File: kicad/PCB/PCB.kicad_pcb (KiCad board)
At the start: 2 copper layers, 80 x 55 mm, 53 parts, among them J1 JST_2mm, J2 JST_2mm, J3 3.5mm, J5 3.5mm, J6 3.5mm, J7 3.5mm, J9 Selector_TC4420, Q1 IRL520N, SW1 SW_DIP_x03, U1 XIAO-RP2350-DIP, U2 AP2112K-3.3, U3 TB6612FNG, U4 TC4420

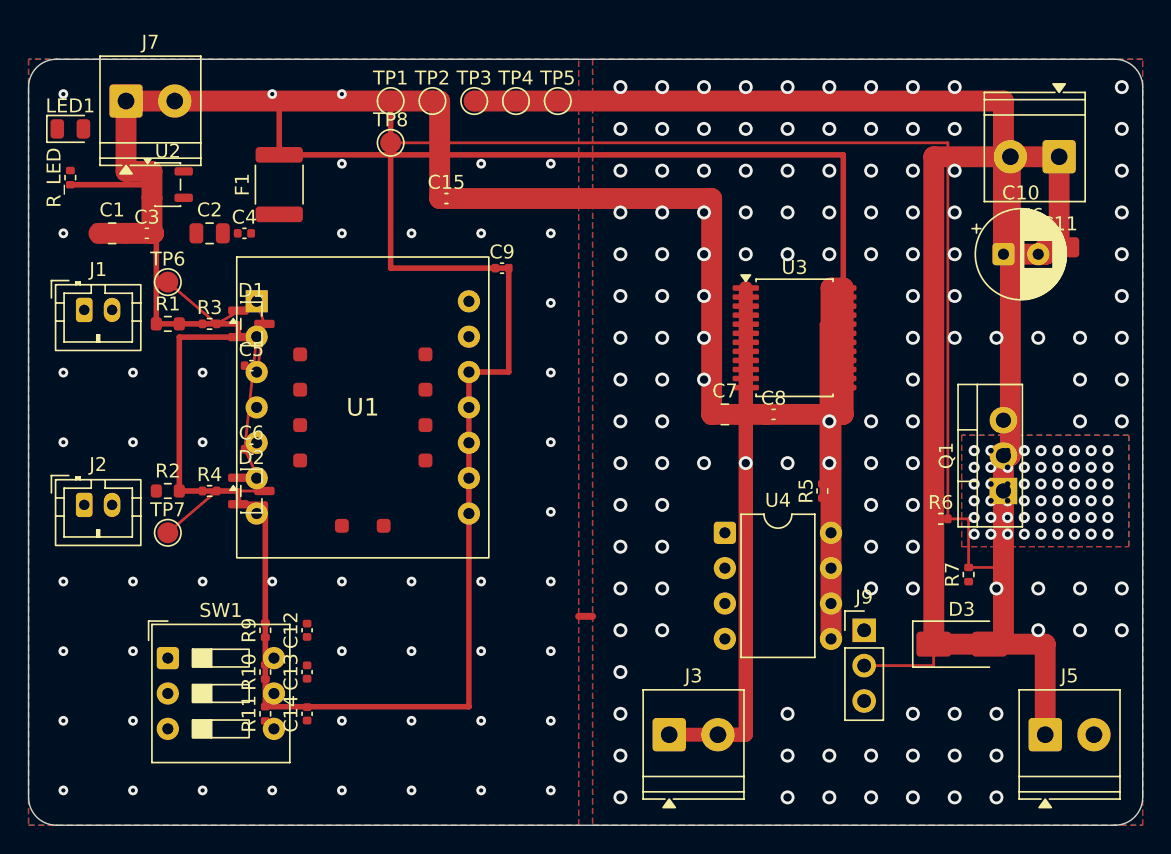
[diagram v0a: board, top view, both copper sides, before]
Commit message: Limpieza de archivos innecesarios de PCB y creacion de guia de enrutado
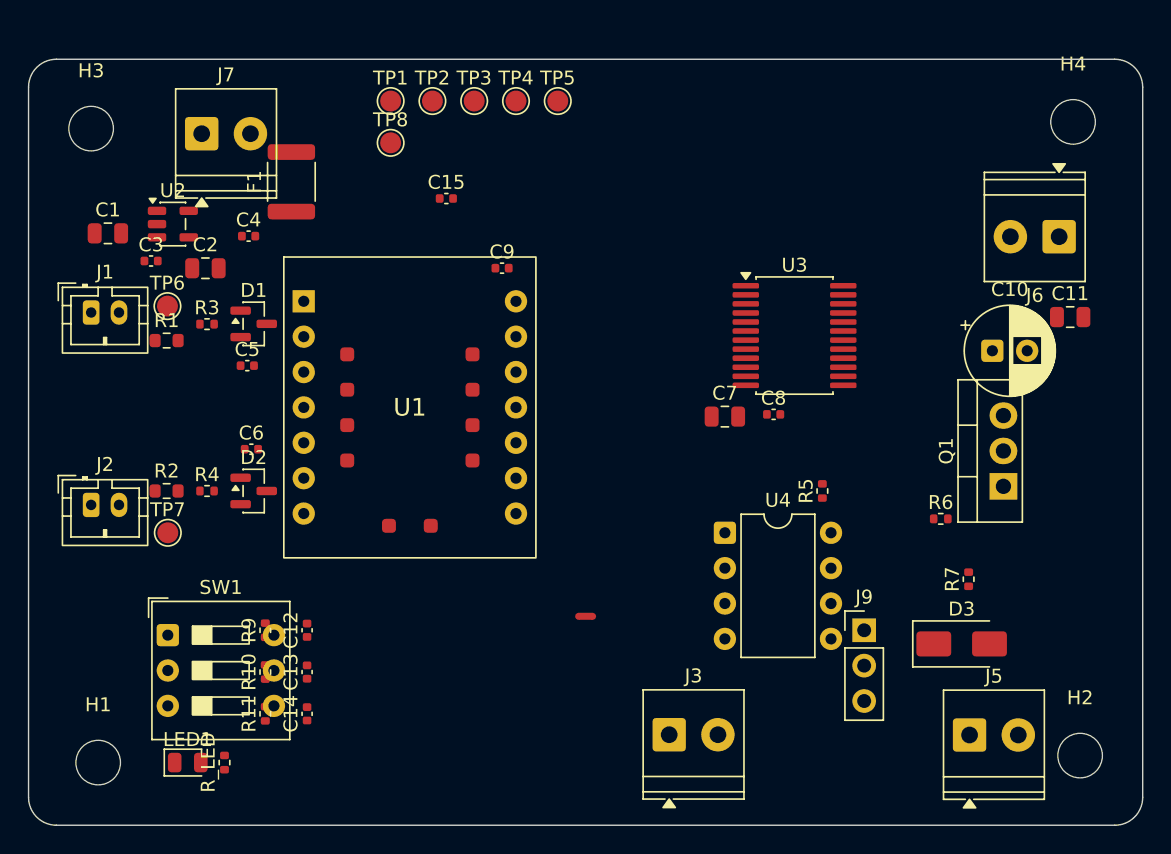
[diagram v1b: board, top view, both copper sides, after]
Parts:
- added H1: MountingHole_3.2mm_M3, MountingHole_3.2mm_M3, F.Cu at (25.0, 70.5)
- added H2: MountingHole_3.2mm_M3, MountingHole_3.2mm_M3, F.Cu at (95.5, 70.0)
- added H3: MountingHole_3.2mm_M3, MountingHole_3.2mm_M3, F.Cu at (24.5, 25.0)
- added H4: MountingHole_3.2mm_M3, MountingHole_3.2mm_M3, F.Cu at (95.0, 24.5)
- moved LED1 46.3 mm to (31.4, 70.5)
- moved R_LED 43.4 mm to (34.1, 70.5)
- moved C10 6.98 mm to (89.2, 40.9)
- moved J7 5.92 mm to (32.4, 25.3)
- moved J6 5.74 mm to (94.0, 32.7)
- moved J5 5.43 mm to (87.6, 68.5)
- moved C11 5.07 mm to (94.8, 38.5)
- moved U1 3.38 mm to (47.4, 45.0)
- moved U2 2.86 mm to (30.4, 31.8)
- moved C2 2.52 mm to (32.7, 35.0)
- moved C3 2.01 mm to (28.8, 34.5)
- moved TP6 1.73 mm to (30.0, 37.7)
- moved SW1 1.65 mm to (30.0, 61.3)
- moved R1 1.20 mm to (29.9, 40.2)
- moved F1 0.90 mm to (38.9, 28.8)
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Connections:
- U1 pad 10: /NET_MOTOR_EN -> /NET_VENT
- U1 pad 11: /NET_VENT -> /NET_MOTOR_EN
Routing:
- net /+3V3: track 207.9 -> 0.00 mm
- net /+5V: track 124.6 -> 0.00 mm
- net /+48V: track 118.5 -> 0.00 mm
- net /NET_Q1_GATE: track 80.0 -> 0.00 mm
- net /NET_AO1: track 37.6 -> 0.00 mm
- net /NET_FAN_HS: track 36.5 -> 0.00 mm
- net /NET_AO2: track 31.5 -> 0.00 mm
- net /NET_TEMP_EXT_FILT: track 19.5 -> 0.00 mm
- net /NET_VENT_GATE: track 15.5 -> 0.00 mm
- net /NET_TEMP_INT_FILT: track 12.7 -> 0.00 mm
- net /PGND: vias 181 -> 0
- net /AGND: vias 49 -> 0
- removed copper zone on B.Cu, net /AGND
- removed copper zone on F.Cu, net /AGND
- removed copper zone on B.Cu, net /PGND
- removed copper zone on F.Cu, net /PGND
